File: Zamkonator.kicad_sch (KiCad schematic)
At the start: 4 parts, among them J1 Screw_Terminal_01x06, J3 Conn_01x08_Male, J4 Conn_02x08_Counter_Clockwise

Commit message: layout fixes
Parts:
- J3: footprint TerminalBlock_Phoenix:TerminalBlock_Phoenix_MPT-0,5-8-2.54_1x08_P2.54mm_Horizontal -> Connector_PinSocket_2.54mm:PinSocket_1x08_P2.54mm_Vertical
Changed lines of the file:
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@@
     (property "Reference" "J3" (id 0) (at 170.815 47.625 90))
     (property "Value" "Conn_01x08_Male" (id 1) (at 170.815 50.165 90))
-    (property "Footprint" "TerminalBlock_Phoenix:TerminalBlock_Phoenix_MPT-0,5-8-2.54_1x08_P2.54mm_Horizontal" (id 2) (at 172.085 52.705 0)
+    (property "Footprint" "Connector_PinSocket_2.54mm:PinSocket_1x08_P2.54mm_Vertical" (id 2) (at 172.085 52.705 0)
       (effects (font (size 1.27 1.27)) hide)
     )
@@
     )
     (path "/8f37bbe0-86b5-4d99-ba58-4681edf3128e/9fe49712-d1e9-4612-8d45-64df3379aa1f"
-      (reference "C27") (unit 1) (value "220u 25V") (footprint "Capacitor_SMD:C_0603_1608Metric_Pad1.08x0.95mm_HandSolder")
+      (reference "C27") (unit 1) (value "220u 25V") (footprint "Capacitor_Tantalum_SMD:CP_EIA-7343-30_AVX-N_Pad2.25x2.55mm_HandSolder")
     )
     (path "/8f37bbe0-86b5-4d99-ba58-4681edf3128e/a5870b19-f323-437d-b9aa-beeddc624810"
@@
     )
     (path "/ae3c1ce2-d60d-4c32-b4eb-1dde79f4bdfe"
-      (reference "J3") (unit 1) (value "Conn_01x08_Male") (footprint "TerminalBlock_Phoenix:TerminalBlock_Phoenix_MPT-0,5-8-2.54_1x08_P2.54mm_Horizontal")
+      (reference "J3") (unit 1) (value "Conn_01x08_Male") (footprint "Connector_PinSocket_2.54mm:PinSocket_1x08_P2.54mm_Vertical")
     )
     (path "/13e0cb8f-9666-43d2-8c06-697a8626a70b"
@@
       (reference "U8") (unit 2) (value "LTV-827S") (footprint "Package_DIP:SMDIP-8_W9.53mm")
     )
-    (path "/2418ed7a-6668-472e-9550-09c70e5c9c72/8be517ba-7de0-424c-8bf1-88ceee2c8b95"
+    (path "/2418ed7a-6668-472e-9550-09c70e5c9c72/a1bb4e35-f679-4c14-9be8-084bdaa69691"
       (reference "X1") (unit 1) (value "S3D50.000000B20F30T") (footprint "project specific:XTAL_TSX-3225_16.0000MF18X-AC3")
     )

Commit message: Finish basic layout
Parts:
- J3: footprint Connector_PinSocket_2.54mm:PinSocket_1x08_P2.54mm_Vertical -> Connector_PinHeader_2.54mm:PinHeader_1x08_P2.54mm_Vertical
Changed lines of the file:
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@@
     (property "Reference" "J3" (id 0) (at 170.815 47.625 90))
     (property "Value" "Conn_01x08_Male" (id 1) (at 170.815 50.165 90))
-    (property "Footprint" "Connector_PinSocket_2.54mm:PinSocket_1x08_P2.54mm_Vertical" (id 2) (at 172.085 52.705 0)
+    (property "Footprint" "Connector_PinHeader_2.54mm:PinHeader_1x08_P2.54mm_Vertical" (id 2) (at 172.085 52.705 0)
       (effects (font (size 1.27 1.27)) hide)
     )
@@
     )
     (path "/ae3c1ce2-d60d-4c32-b4eb-1dde79f4bdfe"
-      (reference "J3") (unit 1) (value "Conn_01x08_Male") (footprint "Connector_PinSocket_2.54mm:PinSocket_1x08_P2.54mm_Vertical")
+      (reference "J3") (unit 1) (value "Conn_01x08_Male") (footprint "Connector_PinHeader_2.54mm:PinHeader_1x08_P2.54mm_Vertical")
     )
     (path "/13e0cb8f-9666-43d2-8c06-697a8626a70b"

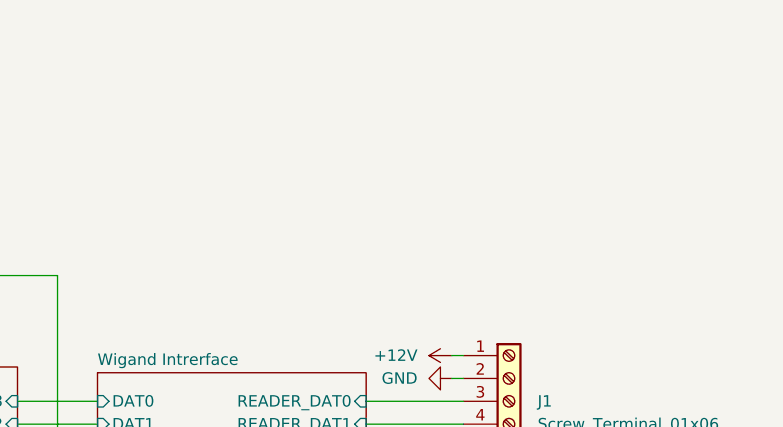
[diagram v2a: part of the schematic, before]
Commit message: add screw holes
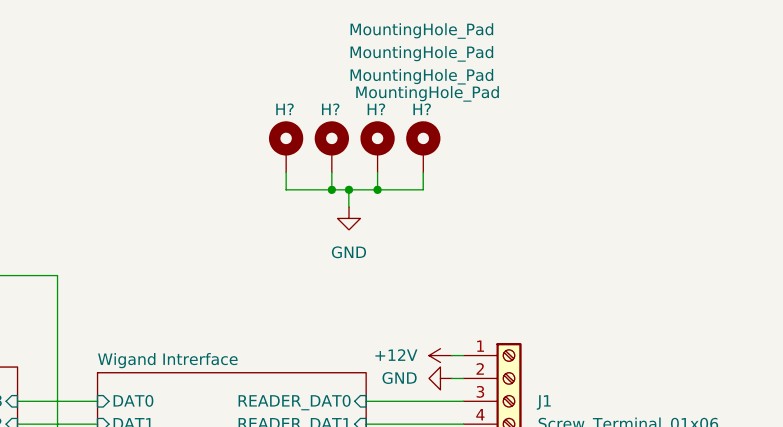
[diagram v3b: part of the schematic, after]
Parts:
- added H? (x4): MountingHole_Pad, symbol Mechanical:MountingHole_Pad
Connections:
- net GND: now also H?.1, H?.1, H?.1, H?.1
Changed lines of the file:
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@@
   (junction (at 200.025 85.09) (diameter 0) (color 0 0 0 0)
   )
+  (junction (at 233.045 56.515) (diameter 0) (color 0 0 0 0)
+  )
   (junction (at 58.42 115.57) (diameter 0) (color 0 0 0 0)
   )
@@
   (junction (at 202.565 107.95) (diameter 0) (color 0 0 0 0)
   )
+  (junction (at 238.125 56.515) (diameter 0) (color 0 0 0 0)
+  )
+  (junction (at 234.95 56.515) (diameter 0) (color 0 0 0 0)
+  )
   (junction (at 59.055 81.915) (diameter 0) (color 0 0 0 0)
   )
@@
   (junction (at 182.245 141.605) (diameter 0) (color 0 0 0 0)
   )
+  (wire (pts (xy 234.95 58.42) (xy 234.95 56.515))
+    (stroke (width 0) (type default) (color 0 0 0 0))
+  )
   (wire (pts (xy 155.575 80.645) (xy 155.575 66.675))
     (stroke (width 0) (type default) (color 0 0 0 0))
@@
     (stroke (width 0) (type default) (color 0 0 0 0))
   )
+  (wire (pts (xy 234.95 56.515) (xy 233.045 56.515))
+    (stroke (width 0) (type default) (color 0 0 0 0))
+  )
+  (wire (pts (xy 227.965 56.515) (xy 227.965 54.61))
+    (stroke (width 0) (type default) (color 0 0 0 0))
+  )
   (wire (pts (xy 164.465 118.745) (xy 164.465 123.19))
     (stroke (width 0) (type default) (color 0 0 0 0))
@@
     (stroke (width 0) (type default) (color 0 0 0 0))
   )
+  (wire (pts (xy 238.125 54.61) (xy 238.125 56.515))
+    (stroke (width 0) (type default) (color 0 0 0 0))
+  )
   (wire (pts (xy 203.835 87.63) (xy 207.01 87.63))
     (stroke (width 0) (type default) (color 0 0 0 0))
@@
     (stroke (width 0) (type default) (color 0 0 0 0))
   )
+  (wire (pts (xy 233.045 54.61) (xy 233.045 56.515))
+    (stroke (width 0) (type default) (color 0 0 0 0))
+  )
   (wire (pts (xy 154.305 121.285) (xy 167.005 121.285))
     (stroke (width 0) (type default) (color 0 0 0 0))
@@
     (stroke (width 0) (type default) (color 0 0 0 0))
   )
+  (wire (pts (xy 238.125 56.515) (xy 243.205 56.515))
+    (stroke (width 0) (type default) (color 0 0 0 0))
+  )
+  (wire (pts (xy 234.95 56.515) (xy 238.125 56.515))
+    (stroke (width 0) (type default) (color 0 0 0 0))
+  )
   (wire (pts (xy 200.025 85.09) (xy 200.025 150.495))
     (stroke (width 0) (type default) (color 0 0 0 0))
@@
     (stroke (width 0) (type default) (color 0 0 0 0))
   )
+  (wire (pts (xy 243.205 56.515) (xy 243.205 54.61))
+    (stroke (width 0) (type default) (color 0 0 0 0))
+  )
   (wire (pts (xy 132.715 94.615) (xy 158.115 94.615))
     (stroke (width 0) (type default) (color 0 0 0 0))
@@
   )
   (wire (pts (xy 55.88 81.915) (xy 59.055 81.915))
+    (stroke (width 0) (type default) (color 0 0 0 0))
+  )
+  (wire (pts (xy 233.045 56.515) (xy 227.965 56.515))
     (stroke (width 0) (type default) (color 0 0 0 0))
   )
@@
     (pin "1")
   )
+  (symbol (lib_name "GND_1") (lib_id "power:GND") (at 234.95 58.42 0) (unit 1)
+    (in_bom yes) (on_board yes) (fields_autoplaced)
+    (property "Reference" "#PWR?" (id 0) (at 234.95 64.77 0)
+      (effects (font (size 1.27 1.27)) hide)
+    )
+    (property "Value" "GND" (id 1) (at 234.95 63.5 0))
+    (property "Footprint" "" (id 2) (at 234.95 58.42 0)
+      (effects (font (size 1.27 1.27)) hide)
+    )
+    (property "Datasheet" "" (id 3) (at 234.95 58.42 0)
+      (effects (font (size 1.27 1.27)) hide)
+    )
+    (pin "1")
+  )
+  (symbol (lib_id "Mechanical:MountingHole_Pad") (at 238.125 52.07 0) (unit 1)
+    (in_bom yes) (on_board yes)
+    (property "Reference" "H?" (id 0) (at 236.855 47.625 0)
+      (effects (font (size 1.27 1.27)) (justify left))
+    )
+    (property "Value" "MountingHole_Pad" (id 1) (at 234.95 43.815 0)
+      (effects (font (size 1.27 1.27)) (justify left))
+    )
+    (property "Footprint" "" (id 2) (at 238.125 52.07 0)
+      (effects (font (size 1.27 1.27)) hide)
+    )
+    (property "Datasheet" "~" (id 3) (at 238.125 52.07 0)
+      (effects (font (size 1.27 1.27)) hide)
+    )
+    (pin "1")
+  )
   (symbol (lib_id "power:+3.3V") (at 19.685 77.47 0) (unit 1)
     (in_bom yes) (on_board yes) (fields_autoplaced)
@@
     (pin "8")
   )
+  (symbol (lib_id "Mechanical:MountingHole_Pad") (at 233.045 52.07 0) (unit 1)
+    (in_bom yes) (on_board yes)
+    (property "Reference" "H?" (id 0) (at 231.775 47.625 0)
+      (effects (font (size 1.27 1.27)) (justify left))
+    )
+    (property "Value" "MountingHole_Pad" (id 1) (at 235.585 45.72 0)
+      (effects (font (size 1.27 1.27)) (justify left))
+    )
+    (property "Footprint" "" (id 2) (at 233.045 52.07 0)
+      (effects (font (size 1.27 1.27)) hide)
+    )
+    (property "Datasheet" "~" (id 3) (at 233.045 52.07 0)
+      (effects (font (size 1.27 1.27)) hide)
+    )
+    (pin "1")
+  )
+  (symbol (lib_id "Mechanical:MountingHole_Pad") (at 243.205 52.07 0) (unit 1)
+    (in_bom yes) (on_board yes)
+    (property "Reference" "H?" (id 0) (at 241.935 47.625 0)
+      (effects (font (size 1.27 1.27)) (justify left))
+    )
+    (property "Value" "MountingHole_Pad" (id 1) (at 234.95 38.735 0)
+      (effects (font (size 1.27 1.27)) (justify left))
+    )
+    (property "Footprint" "" (id 2) (at 243.205 52.07 0)
+      (effects (font (size 1.27 1.27)) hide)
+    )
+    (property "Datasheet" "~" (id 3) (at 243.205 52.07 0)
+      (effects (font (size 1.27 1.27)) hide)
+    )
+    (pin "1")
+  )
   (symbol (lib_id "power:+3.3V") (at 181.61 64.135 270) (unit 1)
     (in_bom yes) (on_board yes) (fields_autoplaced)
@@
     )
     (property "Datasheet" "" (id 3) (at 182.245 143.51 0)
+      (effects (font (size 1.27 1.27)) hide)
+    )
+    (pin "1")
+  )
+  (symbol (lib_id "Mechanical:MountingHole_Pad") (at 227.965 52.07 0) (unit 1)
+    (in_bom yes) (on_board yes)
+    (property "Reference" "H?" (id 0) (at 226.695 47.625 0)
+      (effects (font (size 1.27 1.27)) (justify left))
+    )
+    (property "Value" "MountingHole_Pad" (id 1) (at 234.95 41.275 0)
+      (effects (font (size 1.27 1.27)) (justify left))
+    )
+    (property "Footprint" "" (id 2) (at 227.965 52.07 0)
+      (effects (font (size 1.27 1.27)) hide)
+    )
+    (property "Datasheet" "~" (id 3) (at 227.965 52.07 0)
       (effects (font (size 1.27 1.27)) hide)
     )
@@
       (reference "#PWR0105") (unit 1) (value "GND") (footprint "")
     )
+    (path "/6ab36dc8-2765-4b7a-ac9f-59a7516ee0c9"
+      (reference "#PWR?") (unit 1) (value "GND") (footprint "")
+    )
     (path "/0599421a-f0cb-4879-9da8-2ed04adba3ce/b023df16-89a0-44f8-b620-c618db9e4a0e"
       (reference "C1") (unit 1) (value "47u") (footprint "Capacitor_SMD:C_0603_1608Metric_Pad1.08x0.95mm_HandSolder")
@@
       (reference "D10") (unit 1) (value "1N4007") (footprint "Diode_SMD:D_SMA_Handsoldering")
     )
+    (path "/6e38ed9d-b711-4183-a359-a7eded752fbf"
+      (reference "H?") (unit 1) (value "MountingHole_Pad") (footprint "")
+    )
+    (path "/af3b97a5-5706-4bce-aa78-9a28c006c670"
+      (reference "H?") (unit 1) (value "MountingHole_Pad") (footprint "")
+    )
+    (path "/c038bbc1-1357-445e-9611-4290e0c7d653"
+      (reference "H?") (unit 1) (value "MountingHole_Pad") (footprint "")
+    )
+    (path "/ed028664-426c-4ef4-8cdf-a6eb975ce305"
+      (reference "H?") (unit 1) (value "MountingHole_Pad") (footprint "")
+    )
     (path "/27509945-1925-4d26-9dbb-7ec0ad9cee83"

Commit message: tracks
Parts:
- H1, H2, H3, H4: renamed from H?; footprint (none) -> MountingHole:MountingHole_3.2mm_M3_Pad_Via
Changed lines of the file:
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@@
+    (stroke (width 0) (type default) (color 0 0 0 0))
+  )
+  (wire (pts (xy 205.74 39.37) (xy 212.09 39.37))
     (stroke (width 0) (type default) (color 0 0 0 0))
   )
@@
     (stroke (width 0) (type default) (color 0 0 0 0))
   )
+  (wire (pts (xy 205.74 37.465) (xy 205.74 39.37))
+    (stroke (width 0) (type default) (color 0 0 0 0))
+  )
   (wire (pts (xy 177.165 141.605) (xy 177.165 135.89))
     (stroke (width 0) (type default) (color 0 0 0 0))
@@
   )
   (wire (pts (xy 198.12 107.95) (xy 202.565 107.95))
+    (stroke (width 0) (type default) (color 0 0 0 0))
+  )
+  (wire (pts (xy 212.09 39.37) (xy 212.09 37.465))
     (stroke (width 0) (type default) (color 0 0 0 0))
   )
@@
     )
     (property "Datasheet" "" (id 3) (at 240.665 110.49 0)
+      (effects (font (size 1.27 1.27)) hide)
+    )
+    (pin "1")
+  )
+  (symbol (lib_name "+3.3V_1") (lib_id "power:+3.3V") (at 212.09 37.465 0) (unit 1)
+    (in_bom yes) (on_board yes)
+    (property "Reference" "#PWR?" (id 0) (at 212.09 41.275 0)
+      (effects (font (size 1.27 1.27)) hide)
+    )
+    (property "Value" "+3.3V" (id 1) (at 212.09 32.385 0))
+    (property "Footprint" "" (id 2) (at 212.09 37.465 0)
+      (effects (font (size 1.27 1.27)) hide)
+    )
+    (property "Datasheet" "" (id 3) (at 212.09 37.465 0)
       (effects (font (size 1.27 1.27)) hide)
     )
@@
   (symbol (lib_name "GND_1") (lib_id "power:GND") (at 234.95 58.42 0) (unit 1)
     (in_bom yes) (on_board yes) (fields_autoplaced)
-    (property "Reference" "#PWR?" (id 0) (at 234.95 64.77 0)
+    (property "Reference" "#PWR0106" (id 0) (at 234.95 64.77 0)
       (effects (font (size 1.27 1.27)) hide)
     )
@@
   (symbol (lib_id "Mechanical:MountingHole_Pad") (at 238.125 52.07 0) (unit 1)
     (in_bom yes) (on_board yes)
-    (property "Reference" "H?" (id 0) (at 236.855 47.625 0)
+    (property "Reference" "H3" (id 0) (at 236.855 47.625 0)
       (effects (font (size 1.27 1.27)) (justify left))
     )
@@
       (effects (font (size 1.27 1.27)) (justify left))
     )
-    (property "Footprint" "" (id 2) (at 238.125 52.07 0)
+    (property "Footprint" "MountingHole:MountingHole_3.2mm_M3_Pad_Via" (id 2) (at 238.125 52.07 0)
       (effects (font (size 1.27 1.27)) hide)
     )
@@
   (symbol (lib_id "Mechanical:MountingHole_Pad") (at 233.045 52.07 0) (unit 1)
     (in_bom yes) (on_board yes)
-    (property "Reference" "H?" (id 0) (at 231.775 47.625 0)
+    (property "Reference" "H2" (id 0) (at 231.775 47.625 0)
       (effects (font (size 1.27 1.27)) (justify left))
     )
@@
       (effects (font (size 1.27 1.27)) (justify left))
     )
-    (property "Footprint" "" (id 2) (at 233.045 52.07 0)
+    (property "Footprint" "MountingHole:MountingHole_3.2mm_M3_Pad_Via" (id 2) (at 233.045 52.07 0)
       (effects (font (size 1.27 1.27)) hide)
     )
@@
   (symbol (lib_id "Mechanical:MountingHole_Pad") (at 243.205 52.07 0) (unit 1)
     (in_bom yes) (on_board yes)
-    (property "Reference" "H?" (id 0) (at 241.935 47.625 0)
+    (property "Reference" "H4" (id 0) (at 241.935 47.625 0)
       (effects (font (size 1.27 1.27)) (justify left))
     )
@@
       (effects (font (size 1.27 1.27)) (justify left))
     )
-    (property "Footprint" "" (id 2) (at 243.205 52.07 0)
+    (property "Footprint" "MountingHole:MountingHole_3.2mm_M3_Pad_Via" (id 2) (at 243.205 52.07 0)
       (effects (font (size 1.27 1.27)) hide)
     )
@@
   (symbol (lib_id "Mechanical:MountingHole_Pad") (at 227.965 52.07 0) (unit 1)
     (in_bom yes) (on_board yes)
-    (property "Reference" "H?" (id 0) (at 226.695 47.625 0)
+    (property "Reference" "H1" (id 0) (at 226.695 47.625 0)
       (effects (font (size 1.27 1.27)) (justify left))
     )
@@
       (effects (font (size 1.27 1.27)) (justify left))
     )
-    (property "Footprint" "" (id 2) (at 227.965 52.07 0)
+    (property "Footprint" "MountingHole:MountingHole_3.2mm_M3_Pad_Via" (id 2) (at 227.965 52.07 0)
       (effects (font (size 1.27 1.27)) hide)
     )
@@
     )
     (property "Datasheet" "" (id 3) (at 246.38 74.93 0)
+      (effects (font (size 1.27 1.27)) hide)
+    )
+    (pin "1")
+  )
+  (symbol (lib_id "power:+3V3") (at 205.74 37.465 0) (mirror y) (unit 1)
+    (in_bom yes) (on_board yes)
+    (property "Reference" "#PWR?" (id 0) (at 205.74 41.275 0)
+      (effects (font (size 1.27 1.27)) hide)
+    )
+    (property "Value" "+3V3" (id 1) (at 205.74 32.385 0))
+    (property "Footprint" "" (id 2) (at 205.74 37.465 0)
+      (effects (font (size 1.27 1.27)) hide)
+    )
+    (property "Datasheet" "" (id 3) (at 205.74 37.465 0)
       (effects (font (size 1.27 1.27)) hide)
     )
@@
     )
     (path "/6ab36dc8-2765-4b7a-ac9f-59a7516ee0c9"
-      (reference "#PWR?") (unit 1) (value "GND") (footprint "")
+      (reference "#PWR0106") (unit 1) (value "GND") (footprint "")
+    )
+    (path "/102e6b51-f6b1-4f30-9883-787759c82a1a"
+      (reference "#PWR?") (unit 1) (value "+3.3V") (footprint "")
+    )
+    (path "/f83a81ae-a4f4-425c-ba42-a376986ab744"
+      (reference "#PWR?") (unit 1) (value "+3V3") (footprint "")
     )
     (path "/0599421a-f0cb-4879-9da8-2ed04adba3ce/b023df16-89a0-44f8-b620-c618db9e4a0e"
@@
       (reference "D10") (unit 1) (value "1N4007") (footprint "Diode_SMD:D_SMA_Handsoldering")
     )
+    (path "/ed028664-426c-4ef4-8cdf-a6eb975ce305"
+      (reference "H1") (unit 1) (value "MountingHole_Pad") (footprint "MountingHole:MountingHole_3.2mm_M3_Pad_Via")
+    )
+    (path "/af3b97a5-5706-4bce-aa78-9a28c006c670"
+      (reference "H2") (unit 1) (value "MountingHole_Pad") (footprint "MountingHole:MountingHole_3.2mm_M3_Pad_Via")
+    )
     (path "/6e38ed9d-b711-4183-a359-a7eded752fbf"
-      (reference "H?") (unit 1) (value "MountingHole_Pad") (footprint "")
-    )
-    (path "/af3b97a5-5706-4bce-aa78-9a28c006c670"
-      (reference "H?") (unit 1) (value "MountingHole_Pad") (footprint "")
+      (reference "H3") (unit 1) (value "MountingHole_Pad") (footprint "MountingHole:MountingHole_3.2mm_M3_Pad_Via")
     )
     (path "/c038bbc1-1357-445e-9611-4290e0c7d653"
-      (reference "H?") (unit 1) (value "MountingHole_Pad") (footprint "")
-    )
-    (path "/ed028664-426c-4ef4-8cdf-a6eb975ce305"
-      (reference "H?") (unit 1) (value "MountingHole_Pad") (footprint "")
+      (reference "H4") (unit 1) (value "MountingHole_Pad") (footprint "MountingHole:MountingHole_3.2mm_M3_Pad_Via")
     )
     (path "/27509945-1925-4d26-9dbb-7ec0ad9cee83"

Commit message: Finish layout
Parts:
- removed J4: Conn_02x08_Counter_Clockwise, Connector_PinHeader_2.54mm:PinHeader_2x08_P2.54mm_Vertical, symbol Connector_Generic:Conn_02x08_Counter_Clockwise
- added J4: Conn_02x06_Counter_Clockwise, Connector_PinHeader_2.54mm:PinHeader_2x06_P2.54mm_Vertical, symbol Connector_Generic:Conn_02x06_Counter_Clockwise
- added JP1: SolderJumper_2_Open, Jumper:SolderJumper-2_P1.3mm_Open_RoundedPad1.0x1.5mm, symbol Jumper:SolderJumper_2_Open
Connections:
- net ESP32/IO35 is gone; now on net ESP32/IO18: J3.3 (Pin_3)
- net +12V: now also J1.5 (Pin_5), JP1.1 (A); no longer J1.1 (Pin_1)
- net +3.3V: now also J4.4 (Pin_4), J4.5 (Pin_5)
- net 50MHZ CLOCK/CLK_EN: now also J4.8 (Pin_8)
- net ESP32/IO12: now also J4.1 (Pin_1)
- net ESP32/IO13: now also J4.10 (Pin_10)
- net ESP32/IO15: now also J4.7 (Pin_7)
- net ESP32/IO2: now also J4.2 (Pin_2)
- net ESP32/IO23: now also J4.9 (Pin_9)
- net ESP32/IO5: now also J4.11 (Pin_11)
- net GND: now also J1.6 (Pin_6), J4.6 (Pin_6); no longer J1.2 (Pin_2)
- net Wigand Intrerface/READER_BUZZER: now also J1.2 (Pin_2); no longer J1.6 (Pin_6)
- net Wigand Intrerface/READER_LED: now also J1.1 (Pin_1); no longer J1.5 (Pin_5)
- new net: J4.3 (Pin_3), JP1.2 (B)
- new net ESP32/IO4: J4.12 (Pin_12)
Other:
- sheet ESP32 ports: added none; removed IO32, IO33, IO34, IO35
- moved on the sheet: J1
